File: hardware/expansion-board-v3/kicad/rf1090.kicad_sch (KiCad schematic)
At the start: 49 parts, among them J6 U.FL_1090_EXT(经尾线转SMA), Q3 AO3401A, U11 QPL9547TR7, U12 BGA2817, U13 AD8319ACPZ-R7(主), U14 AD8313ARMZ(备,二选一), U15 TLV3501(TOKMAS), U16 XA17-G4K(或AS179-92LF)

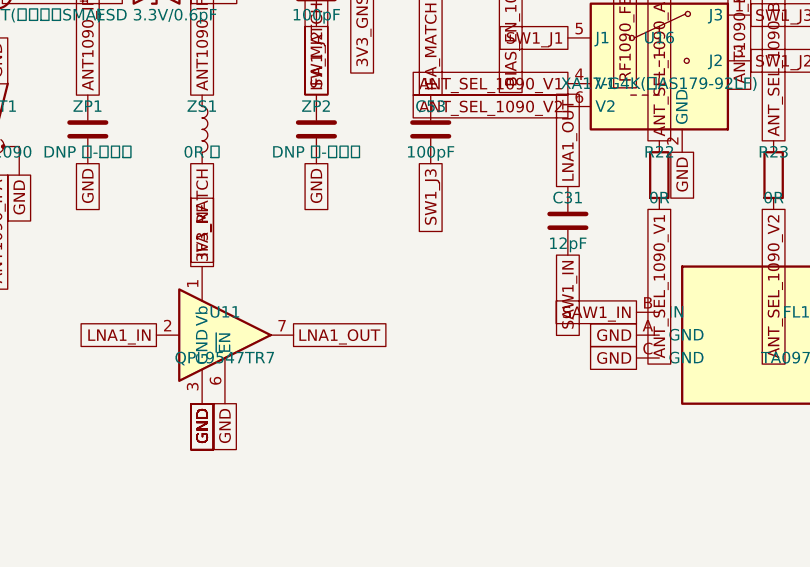
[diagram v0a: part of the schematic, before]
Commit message: feat(hw): 固化六层 IFA 预研模型并集成 v4
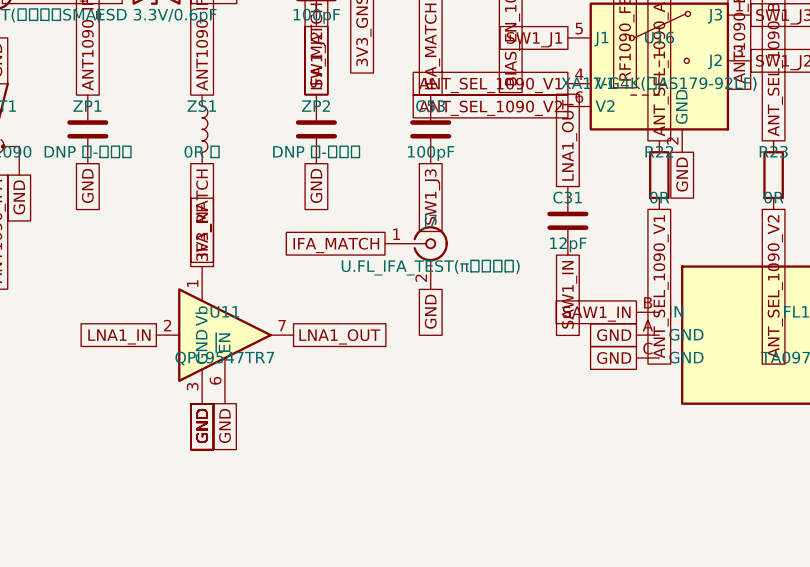
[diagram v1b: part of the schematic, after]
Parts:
- added J7: U.FL_IFA_TEST(π后调试口), Connector_Coaxial:U.FL_Hirose_U.FL-R-SMT-1_Vertical, symbol Connector:Conn_Coaxial
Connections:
- net GND: now also J7.2 (Ext)
- net IFA_MATCH: now also J7.1 (In)
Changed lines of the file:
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@@
+	)
+	(symbol
+		(lib_id "Connector:Conn_Coaxial")
+		(at 86.36 78.74 0)
+		(unit 1)
+		(exclude_from_sim no)
+		(in_bom yes)
+		(on_board yes)
+		(dnp no)
+		(property "Reference" "J7"
+			(at 86.36 76.2 0)
+			(effects (font (size 1.27 1.27)))
+		)
+		(property "Value" "U.FL_IFA_TEST(π后调试口)"
+			(at 86.36 81.28 0)
+			(effects (font (size 1.27 1.27)))
+		)
+		(property "Footprint" "Connector_Coaxial:U.FL_Hirose_U.FL-R-SMT-1_Vertical"
+			(at 86.36 83.82 0)
+			(effects (font (size 1.27 1.27))
+				(hide yes))
+		)
+		(property "Datasheet" "~"
+			(at 86.36 86.36 0)
+			(effects (font (size 1.27 1.27))
+				(hide yes))
+		)
+		(pin "1"
+		)
+		(pin "2"
+		)
+		(instances
+			(project "expansion-board-v3"
+				(path "/10000000-0000-4000-8000-000000000001/20000000-0000-4000-8000-000000000003"
+					(reference "J7")
+					(unit 1)
+				)
+			)
+		)
+	)
+	(global_label "IFA_MATCH"
+		(shape passive)
+		(at 81.28 78.74 180)
+		(effects (font (size 1.27 1.27)) (justify right))
+	)
+	(global_label "GND"
+		(shape passive)
+		(at 86.36 83.82 90)
+		(effects (font (size 1.27 1.27)) (justify right))
 	)
 	(symbol

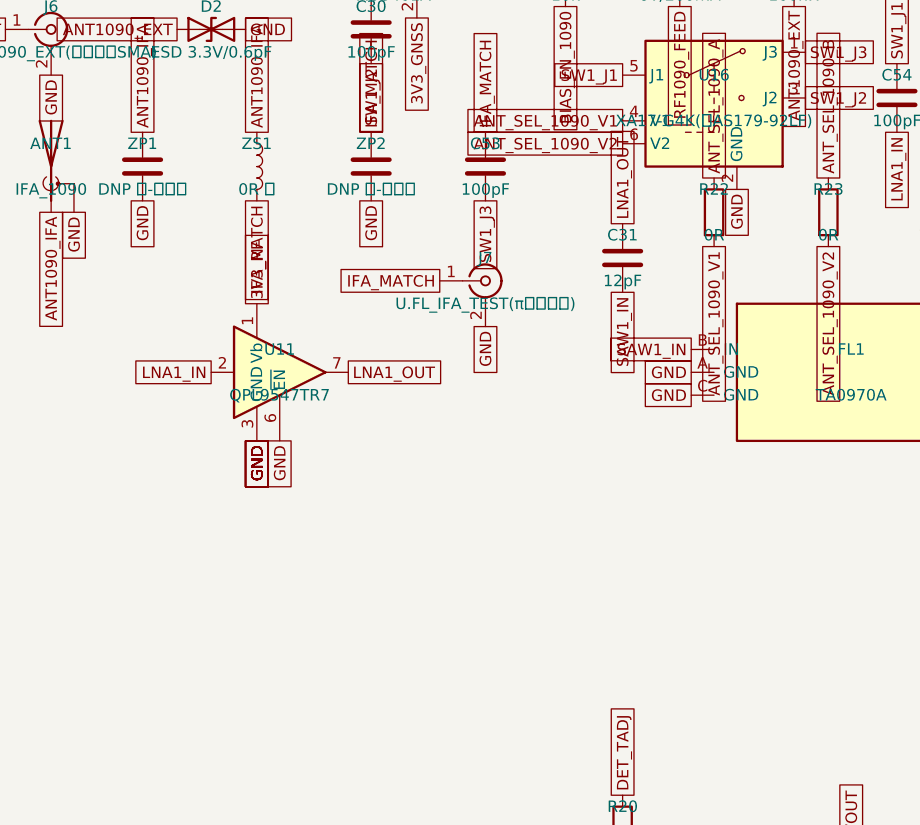
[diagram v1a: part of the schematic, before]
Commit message: fix(v3): correct QPL9547 bias and release V3.8
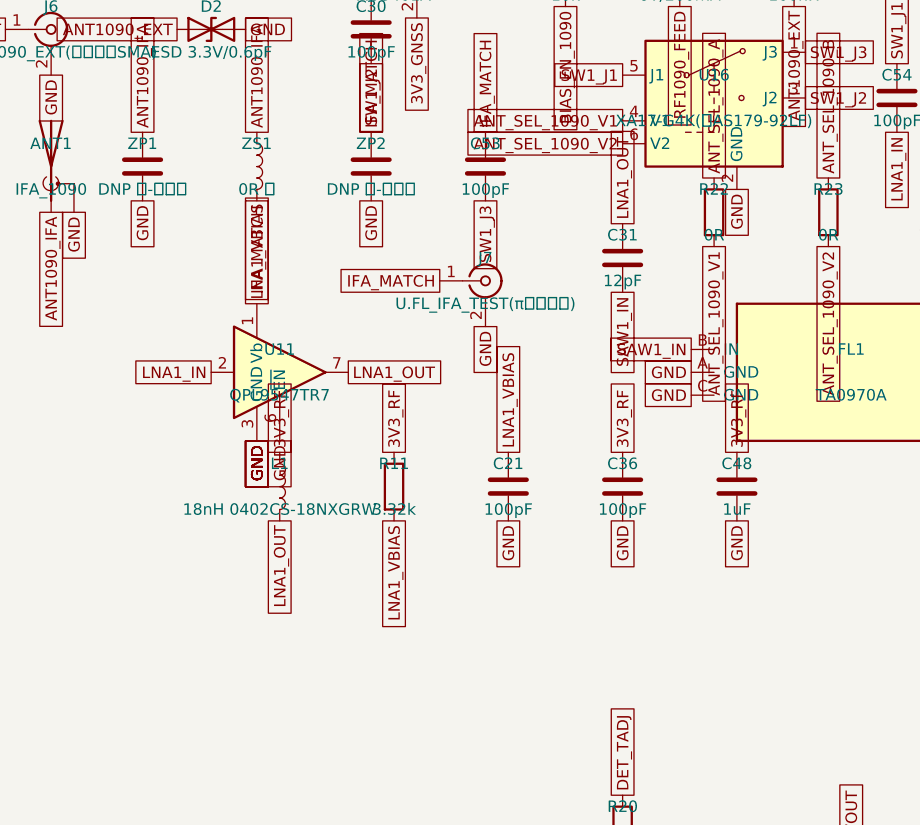
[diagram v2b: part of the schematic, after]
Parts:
- added C21, C36: 100pF, Capacitor_SMD:C_0402_1005Metric, symbol Device:C
- added C48: 1uF, Capacitor_SMD:C_0402_1005Metric, symbol Device:C
- added L1: 18nH 0402CS-18NXGRW, Inductor_SMD:L_0402_1005Metric, symbol Device:L
- added R11: 3.32k, Resistor_SMD:R_0402_1005Metric, symbol Device:R
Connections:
- net 3V3_RF: now also C36.1, C48.1, L1.1, R11.1; no longer U11.1 (Vb)
- net GND: now also C21.2, C36.2, C48.2
- net LNA1_OUT: now also L1.2
- new net LNA1_VBIAS: C21.1, R11.2, U11.1 (Vb)

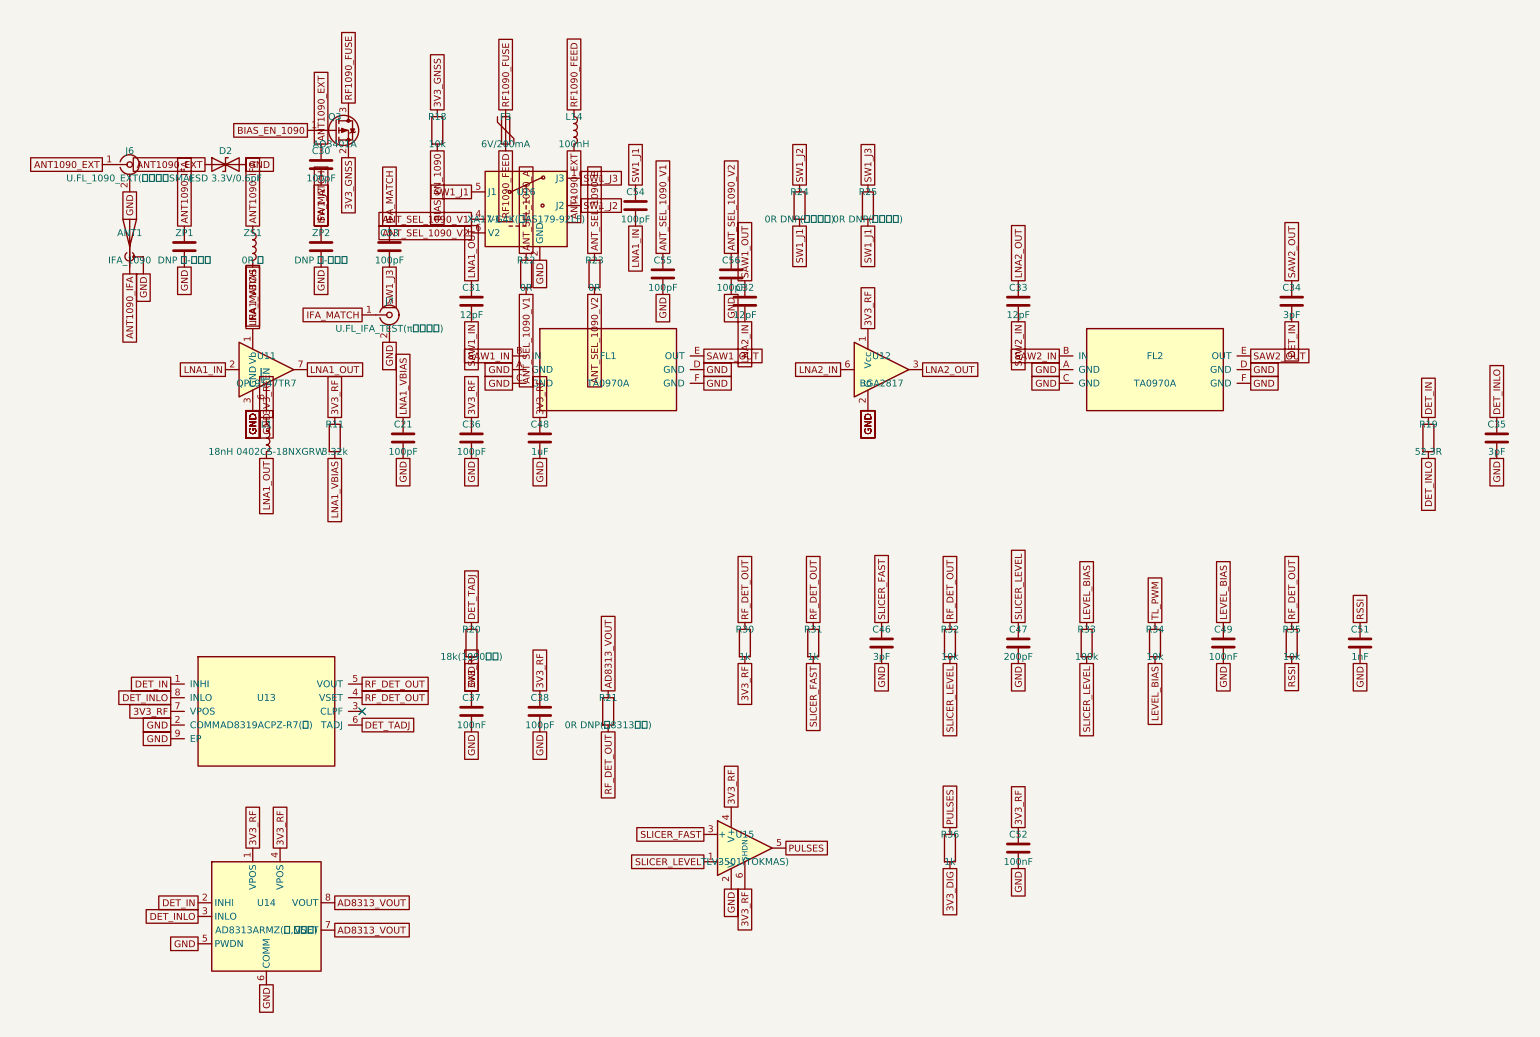
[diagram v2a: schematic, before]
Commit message: feat(v3): backport V4 fixes into a clean V3.9 candidate (phases A-D)
Builds the V3.9 candidate from the V3.8 master rather than from the
working-tree intermediate. The intermediate had the 14 audit parts and a
cleared back side, but had lost 24 board-level silkscreen strings and all
four named RF zones - tools/rebuild.sh starts with gen_pcb.py, which calls
pcbnew.NewBoard(), and neither gr_text nor named zones live in
PLACEMENT.py or ROUTES.json, so every run drops them. The master is the
opposite: intact silkscreen and zones, missing only components. Adding
components back is enumerable (14 designators); restoring 24 silkscreen
strings with correct position, layer, size and mirroring is not.

Coordinates are transplanted from the intermediate, so nothing is
re-placed by hand. What that does cost is copper: the master was routed
without these parts, and 13 of the 18 land on existing tracks. Ripping
those out plus the resulting dangling chains removes 176 segments and 26
vias against the master's 1620/377 - all of it folded into phase E, which
was going to be manual routing anyway. Re-placing 13 parts on a fully
routed board would have been worse; C82-C86 are RP2040 local decouplers
that must stay next to the die, which is exactly how V4.3 ended up with
its 30 mm detour.

Phase B removes the AD8319 experimental branch (U13, R20, DET_TADJ). The
"directional error" turned out to reach into the generators, not just
prose - five places, of which two would have produced wrong hardware:

    gen_bom_smt.py   SKIP_REF = {"U14"}   the only detector excluded
                                          from the pick-and-place BOM
    gen_bom.py       ORDERED listed "AD8313ARMZ(备,二选一)", a suffixed
                     string that never matched the netlist value, so the
                     part had never once been classified

Ordering the V3.8 BOM as it stood would have produced a board whose 1090
receive chain has no detector at all. Phase B's hard criterion now holds:
excluding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
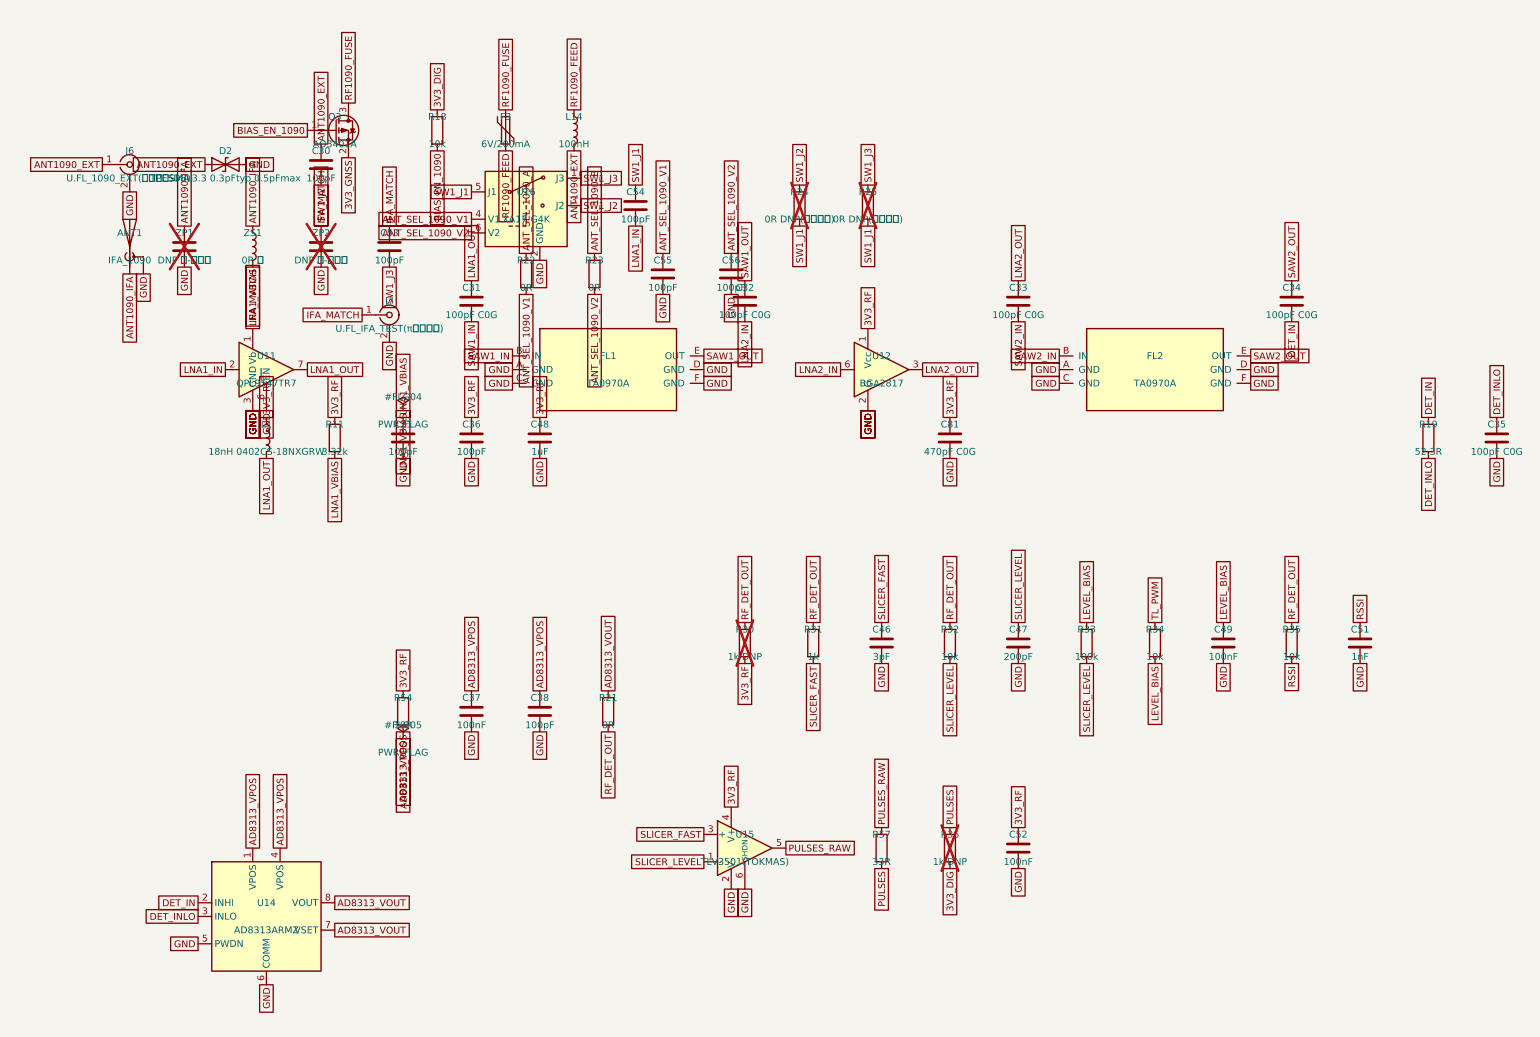
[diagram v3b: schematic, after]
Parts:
- removed R20: 18k(1090实调), Resistor_SMD:R_0603_1608Metric, symbol Device:R
- removed U13: AD8319ACPZ-R7(主), expansion-board-v3:AD8319_LFCSP-8-EP, symbol expansion-board-v3:AD8319
- added C81: 470pF C0G, Capacitor_SMD:C_0402_1005Metric, symbol Device:C
- added R54: 10R, Resistor_SMD:R_0402_1005Metric, symbol Device:R
- added R57: 33R, Resistor_SMD:R_0603_1608Metric, symbol Device:R
- C31, C32, C33: value 12pF -> 100pF C0G
- C34, C35: value 3pF -> 100pF C0G
- D2: value ESD 3.3V/0.6pF -> TPESD8L3.3 0.3pFtyp 0.5pFmax
- R21: value 0R DNP(选8313时贴) -> 0R
- R24, R25, ZP1, ZP2: now not fitted
- R30, R36: value 1k -> 1k DNP; now not fitted
- U14: value AD8313ARMZ(备,二选一) -> AD8313ARMZ
- U16: value XA17-G4K(或AS179-92LF) -> XA17-G4K
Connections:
- net 3V3_DIG: now also R18.1
- net 3V3_GNSS: no longer R18.1
- net 3V3_RF: now also C81.1, R54.1; no longer C37.1, C38.1, U14.1 (VPOS), U14.4 (VPOS), U15.6 (SHDN)
- net GND: now also U15.6 (SHDN), C81.2
- net PULSES: now also R57.2; no longer U15.5
- new net AD8313_VPOS: C37.1, C38.1, R54.2, U14.1 (VPOS), U14.4 (VPOS)
- new net PULSES_RAW: R57.1, U15.5
- no-connect marks 1 -> 0
